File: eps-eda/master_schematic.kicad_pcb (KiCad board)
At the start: 2 copper layers, 96 x 90 mm, 84 parts, among them J1 USB_C_Receptacle, J2 436500212, J3 Conn_02x20_Odd_Even, J4 Conn_01x05_90deg, Q2 FZT688BTA, U1 TPS61022RWUR, U2 TPS61022RWUR, U3 INA3221AIRGVR, U5 MAX77757JEFG435+, U6 MAX17055ETB+T, U7 ATA6560-GAQW-VAO, U8 PIC18F27Q84-E/SP

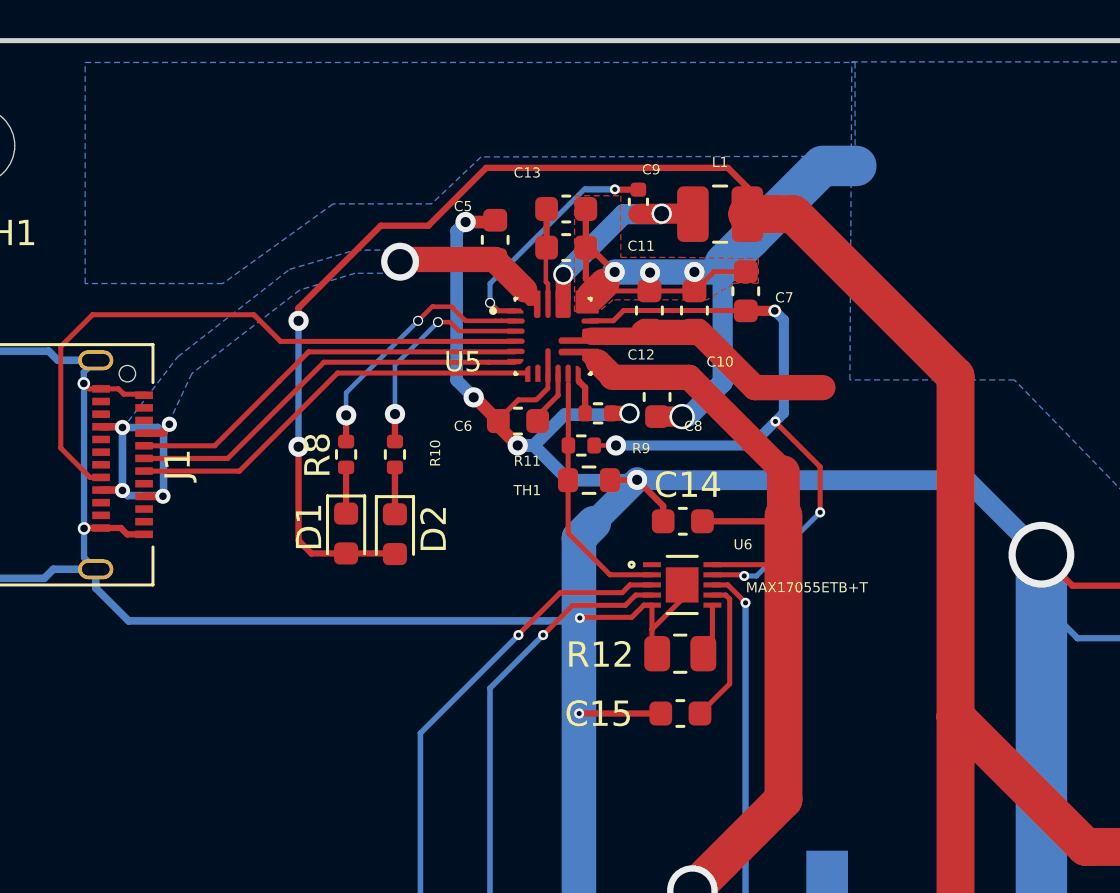
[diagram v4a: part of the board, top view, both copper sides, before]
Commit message: rev 0.2
ran DRC with updated board. rev0.2 complete
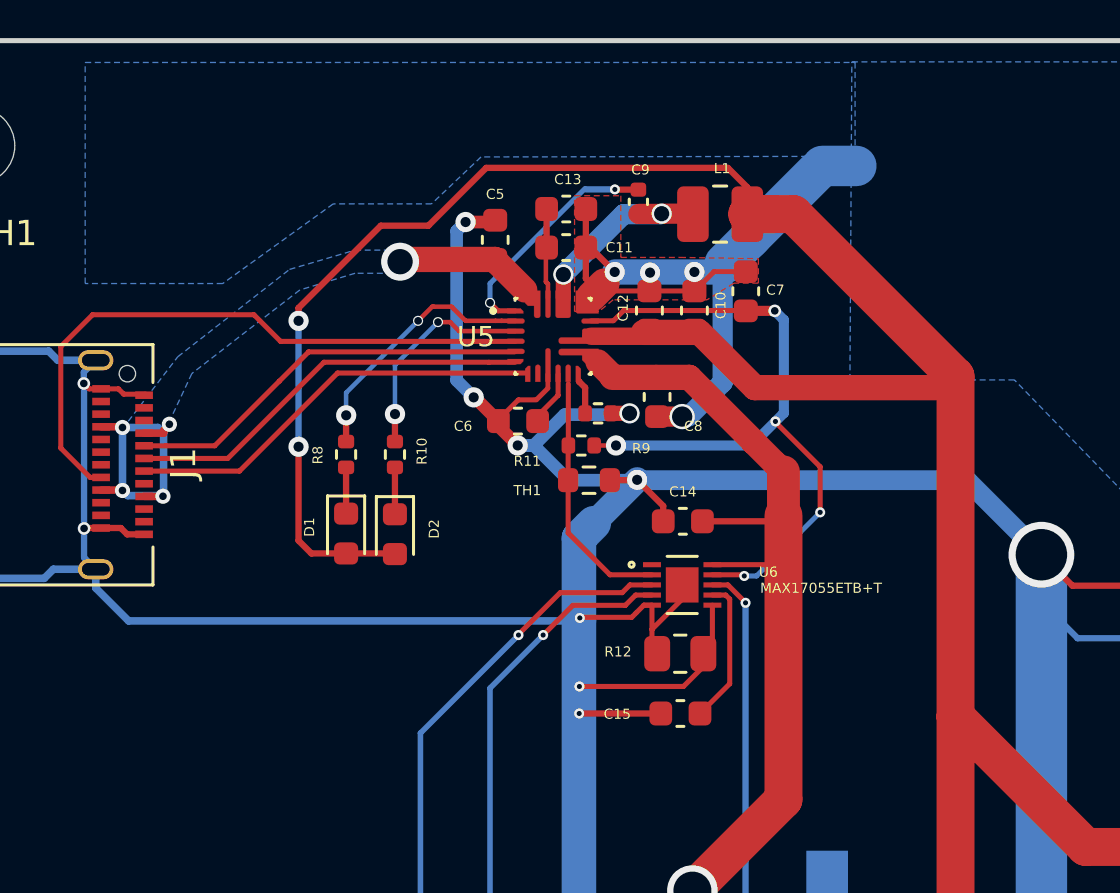
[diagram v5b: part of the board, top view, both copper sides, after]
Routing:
- net GND: track 657.7 -> 663.5 mm, vias 20 -> 21
- net /charge schem/SYSPOWER: track 134.9 -> 140.3 mm
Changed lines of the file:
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@@
     (property "Sheetname" "charge schem")
     (attr smd)
-    (fp_text reference "J1" (at 0 -6.36 90) (layer "F.SilkS")
+    (fp_text reference "J1" (at -0.0508 -6.5786 90) (layer "F.SilkS")
       (effects (font (size 1 1) (thickness 0.15)))
     )
@@
     (property "Sheetname" "charge schem")
     (attr smd)
-    (fp_text reference "C13" (at -1.537 -1.43) (layer "F.SilkS")
+    (fp_text reference "C13" (at 0.0632 -1.1684) (layer "F.SilkS")
       (effects (font (size 0.4 0.4) (thickness 0.1)))
     )
@@
     (property "Sheetname" "charge schem")
     (attr smd)
-    (fp_text reference "C5" (at 1.3208 -1.27 180) (layer "F.SilkS")
+    (fp_text reference "C5" (at 1.8034 0 180) (layer "F.SilkS")
       (effects (font (size 0.4 0.4) (thickness 0.1)))
     )
@@
     (property "Sheetname" "charge schem")
     (attr smd)
-    (fp_text reference "R10" (at 0.0508 1.6002 90) (layer "F.SilkS")
+    (fp_text reference "R10" (at 0.127 1.0668 90) (layer "F.SilkS")
       (effects (font (size 0.4 0.4) (thickness 0.1)))
     )
@@
     (property "Sheetname" "charge schem")
     (attr smd)
-    (fp_text reference "C15" (at 3.2258 -0.0254) (layer "F.SilkS")
-      (effects (font (size 1 1) (thickness 0.15)))
+    (fp_text reference "C15" (at 2.494 -0.0242) (layer "F.SilkS")
+      (effects (font (size 0.4 0.4) (thickness 0.1)))
     )
     (fp_text value "0.47uF" (at 0 1.43) (layer "F.Fab")
@@
     (attr smd)
     (fp_text reference "D2" (at -0.2032 -1.5494 90) (layer "F.SilkS")
-      (effects (font (size 1 1) (thickness 0.15)))
+      (effects (font (size 0.4 0.4) (thickness 0.1)))
     )
     (fp_text value "LED" (at 0 1.43 90) (layer "F.Fab")
@@
     (property "Sheetname" "charge schem")
     (attr smd)
-    (fp_text reference "R12" (at -3.175 0.0508) (layer "F.SilkS")
-      (effects (font (size 1 1) (thickness 0.15)))
+    (fp_text reference "R12" (at -2.4638 -0.0762) (layer "F.SilkS")
+      (effects (font (size 0.4 0.4) (thickness 0.1)))
     )
     (fp_text value "0.010" (at 0 1.65) (layer "F.Fab")
@@
     (property "Sheetname" "charge schem")
     (attr smd)
-    (fp_text reference "C12" (at -1.752 -0.326) (layer "F.SilkS")
+    (fp_text reference "C12" (at 0.1016 -1.0414 90) (layer "F.SilkS")
       (effects (font (size 0.4 0.4) (thickness 0.1)))
     )
@@
     (property "Sheetname" "charge schem")
     (attr through_hole)
-    (fp_text reference "U6" (at 2.4036 -1.5938) (layer "F.SilkS")
+    (fp_text reference "U6" (at 3.4036 -0.508) (layer "F.SilkS")
       (effects (font (size 0.4 0.4) (thickness 0.1)))
     )
-    (fp_text value "MAX17055ETB+T" (at 4.9286 0.1062) (layer "F.SilkS")
+    (fp_text value "MAX17055ETB+T" (at 5.4864 0.127) (layer "F.SilkS")
       (effects (font (size 0.4 0.4) (thickness 0.1)))
     )
@@
     (property "Sheetname" "charge schem")
     (attr smd)
-    (fp_text reference "U5" (at -3.556 1.016) (layer "F.SilkS")
+    (fp_text reference "U5" (at -3.048 0.0254) (layer "F.SilkS")
       (effects (font (size 0.8 0.8) (thickness 0.15)))
     )
@@
     (property "Sheetname" "charge schem")
     (attr smd)
-    (fp_text reference "C9" (at -1.27 -0.508 180) (layer "F.SilkS")
+    (fp_text reference "C9" (at -1.2646 -0.0804 180) (layer "F.SilkS")
       (effects (font (size 0.4 0.4) (thickness 0.1)))
     )
@@
     (property "Sheetname" "charge schem")
     (attr smd)
-    (fp_text reference "C10" (at -2.032 1.016 180) (layer "F.SilkS")
+    (fp_text reference "C10" (at 0.2032 1.0414 270) (layer "F.SilkS")
       (effects (font (size 0.4 0.4) (thickness 0.1)))
     )
@@
     (attr smd)
     (fp_text reference "R8" (at -0.0254 -1.1176 90) (layer "F.SilkS")
-      (effects (font (size 1 1) (thickness 0.15)))
+      (effects (font (size 0.4 0.4) (thickness 0.1)))
     )
     (fp_text value "1k" (at 0 1.17 90) (layer "F.Fab")
@@
     (property "Sheetname" "charge schem")
     (attr smd)
-    (fp_text reference "C11" (at 2.963 -0.0588) (layer "F.SilkS")
+    (fp_text reference "C11" (at 2.0952 0) (layer "F.SilkS")
       (effects (font (size 0.4 0.4) (thickness 0.1)))
     )
@@
     (attr smd)
     (fp_text reference "D1" (at -0.2539 1.4478 90) (layer "F.SilkS")
-      (effects (font (size 1 1) (thickness 0.15)))
+      (effects (font (size 0.4 0.4) (thickness 0.1)))
     )
     (fp_text value "LED" (at 0 1.43 90) (layer "F.Fab")
@@
     (property "Sheetname" "charge schem")
     (attr smd)
-    (fp_text reference "C14" (at -0.2032 1.4292) (layer "F.SilkS")
-      (effects (font (size 1 1) (thickness 0.15)))
+    (fp_text reference "C14" (at 0 1.1684) (layer "F.SilkS")
+      (effects (font (size 0.4 0.4) (thickness 0.1)))
     )
     (fp_text value "0.1uF" (at 0 1.43) (layer "F.Fab")
@@
     (property "Sheetname" "charge schem")
     (attr smd)
-    (fp_text reference "L1" (at 0 -2.05) (layer "F.SilkS")
+    (fp_text reference "L1" (at 0.0762 -1.8034) (layer "F.SilkS")
       (effects (font (size 0.4 0.4) (thickness 0.1)))
     )
@@
     (property "Sheetname" "charge schem")
     (attr smd)
-    (fp_text reference "C7" (at -0.254 1.524 180) (layer "F.SilkS")
+    (fp_text reference "C7" (at 0.0508 1.1684 180) (layer "F.SilkS")
       (effects (font (size 0.4 0.4) (thickness 0.1)))
     )
@@
   (segment (start 46.184 69.644) (end 45.97 69.43) (width 0.2) (layer "F.Cu") (net 1))
   (segment (start 84.425 136.325) (end 83.385 136.325) (width 0.5) (layer "F.Cu") (net 1))
+  (segment (start 70.4577 80.1116) (end 70.4577 80.6215) (width 0.25) (layer "F.Cu") (net 1))
   (segment (start 87.49 125.615) (end 86.505 126.6) (width 0.5) (layer "F.Cu") (net 1))
   (segment (start 68.8718 74.8792) (end 68.8718 74.2718) (width 0.25) (layer "F.Cu") (net 1))
@@
   (segment (start 46.967489 128.196289) (end 46.967489 122.437511) (width 0.25) (layer "F.Cu") (net 1))
   (segment (start 48.391921 69.854479) (end 47.548961 69.854479) (width 0.2) (layer "F.Cu") (net 1))
+  (segment (start 69.6722 81.407) (end 65.5574 81.407) (width 0.2) (layer "F.Cu") (net 1))
   (segment (start 96.25 82.265) (end 94.015 82.265) (width 0.25) (layer "F.Cu") (net 1))
   (segment (start 61.48 111.76) (end 62.185 111.76) (width 0.7) (layer "F.Cu") (net 1))
@@
   (segment (start 52.7942 130.3782) (end 52.8574 130.315) (width 0.25) (layer "F.Cu") (net 1))
   (segment (start 69.6214 77.3938) (end 69.6214 77.9536) (width 0.25) (layer "F.Cu") (net 1))
+  (segment (start 70.4577 80.6215) (end 69.6722 81.407) (width 0.2) (layer "F.Cu") (net 1))
   (segment (start 132.076511 116.290489) (end 130.902 117.465) (width 0.5) (layer "F.Cu") (net 1))
   (segment (start 69.6214 77.9536) (end 68.4276 79.1474) (width 0.2) (layer "F.Cu") (net 1))
@@
   (via (at 45.98 75.16) (size 0.5) (drill 0.3) (layers "F.Cu" "B.Cu") (net 1))
   (via (at 83.82 111.76) (size 1.1) (drill 0.781437) (layers "F.Cu" "B.Cu") (net 1))
+  (via (at 65.5574 81.407) (size 0.4) (drill 0.2) (layers "F.Cu" "B.Cu") (net 1))
   (via (at 94 82.25) (size 0.8) (drill 0.4) (layers "F.Cu" "B.Cu") (net 1))
   (via (at 67.84 73.24) (size 0.8) (drill 0.4) (layers "F.Cu" "B.Cu") (net 1))
@@
   (segment (start 56.3372 76.1492) (end 58.2421 76.1492) (width 0.25) (layer "F.Cu") (net 10))
   (segment (start 93.25 80.75) (end 92.5 81.5) (width 0.25) (layer "F.Cu") (net 10))
+  (segment (start 70.2883 67.3927) (end 72.4916 69.596) (width 1) (layer "F.Cu") (net 10))
   (segment (start 92.5 81.5) (end 92.5 84) (width 0.25) (layer "F.Cu") (net 10))
   (segment (start 80.425 69.1474) (end 80.425 82.6) (width 1.5) (layer "F.Cu") (net 10))
@@
   (segment (start 94.435 83.815) (end 94 84.25) (width 0.25) (layer "F.Cu") (net 10))
   (segment (start 66.016 67.564) (end 68.085 67.564) (width 0.69) (layer "F.Cu") (net 10))
+  (segment (start 79.9764 69.596) (end 80.425 69.1474) (width 1) (layer "F.Cu") (net 10))
   (segment (start 71.4248 60.9092) (end 72.195 61.6794) (width 0.25) (layer "F.Cu") (net 10))
   (segment (start 85.575 87.75) (end 80.425 82.6) (width 1.5) (layer "F.Cu") (net 10))
@@
   (segment (start 97 80.75) (end 93.25 80.75) (width 0.25) (layer "F.Cu") (net 10))
   (segment (start 74.0156 62.738) (end 80.425 69.1474) (width 1.5) (layer "F.Cu") (net 10))
+  (segment (start 72.4916 69.596) (end 79.9764 69.596) (width 1) (layer "F.Cu") (net 10))
   (segment (start 96.274999 83.790001) (end 99.215001 83.790001) (width 0.25) (layer "F.Cu") (net 10))
   (segment (start 68.085 67.564) (end 68.326 67.323) (width 0.25) (layer "F.Cu") (net 10))
   (segment (start 57.7088 63.1952) (end 59.5884 63.1952) (width 0.25) (layer "F.Cu") (net 10))
-  (segment (start 70.2883 67.3927) (end 72.4916 69.596) (width 1) (layer "F.Cu") (net 10))
   (segment (start 96.25 83.815) (end 96.274999 83.790001) (width 0.25) (layer "F.Cu") (net 10))
   (segment (start 72.195 61.6794) (end 72.195 62.738) (width 0.25) (layer "F.Cu") (net 10))
@@
   (segment (start 72.195 62.738) (end 74.0156 62.738) (width 1.5) (layer "F.Cu") (net 10))
   (segment (start 97.79 83.29) (end 97.25 82.75) (width 0.25) (layer "F.Cu") (net 10))
-  (segment (start 72.4916 69.596) (end 75.184 69.596) (width 1) (layer "F.Cu") (net 10))
   (segment (start 94 84.25) (end 94 87.6971) (width 0.25) (layer "F.Cu") (net 10))
   (via (at 54.4576 71.9328) (size 0.8) (drill 0.4) (layers "F.Cu" "B.Cu") (net 10))
